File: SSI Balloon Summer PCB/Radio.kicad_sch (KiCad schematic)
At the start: 16 parts, among them J3 LoRa antenna, J4 APRS antenna, U1 RFM95W-915S2, U5 DRA818V

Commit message: Fixed ERC - no ERC errors
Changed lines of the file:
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@@
 	)
 	(junction
+		(at 116.84 111.76)
+		(diameter 0)
+		(color 0 0 0 0)
+	)
+	(junction
 		(at 196.85 80.01)
 		(diameter 0)
@@
 		)
 	)
+	(label "+4V1"
+		(at 250.19 102.87 0)
+		(effects
+			(font
+				(size 1.27 1.27)
+			)
+			(justify left bottom)
+		)
+	)
 	(label "APRS_AUDIO"
 		(at 147.32 80.01 0)
@@
 	)
 	(symbol
-		(lib_id "power:+4V")
-		(at 250.19 102.87 0)
-		(unit 1)
-		(body_style 1)
-		(exclude_from_sim no)
-		(in_bom yes)
-		(on_board yes)
-		(in_pos_files yes)
-		(dnp no)
-		(fields_autoplaced yes)
-		(property "Reference" "#PWR074"
-			(at 250.19 106.68 0)
-			(hide yes)
-			(show_name no)
-			(do_not_autoplace no)
-			(effects
-				(font
-					(size 1.27 1.27)
-				)
-			)
-		)
-		(property "Value" "+4V1"
-			(at 250.19 97.79 0)
-			(show_name no)
-			(do_not_autoplace no)
-			(effects
-				(font
-					(size 1.27 1.27)
-				)
-			)
-		)
-		(property "Footprint" ""
-			(at 250.19 102.87 0)
-			(hide yes)
-			(show_name no)
-			(do_not_autoplace no)
-			(effects
-				(font
-					(size 1.27 1.27)
-				)
-			)
-		)
-		(property "Datasheet" ""
-			(at 250.19 102.87 0)
-			(hide yes)
-			(show_name no)
-			(do_not_autoplace no)
-			(effects
-				(font
-					(size 1.27 1.27)
-				)
-			)
-		)
-		(property "Description" "Power symbol creates a global label with name \"+4V1\""
-			(at 250.19 102.87 0)
-			(hide yes)
-			(show_name no)
-			(do_not_autoplace no)
-			(effects
-				(font
-					(size 1.27 1.27)
-				)
-			)
-		)
-		(pin "1"
-		)
-		(instances
-			(project "SSI Summer Balloons"
-				(path "/3c45a535-6e6b-4825-ad52-82c10cbe7866/2467bfc8-9a58-45c6-9683-5b5ac73ee36d"
-					(reference "#PWR074")
-					(unit 1)
-				)
-			)
-		)
-	)
-	(symbol
 		(lib_id "power:GND")
 		(at 201.93 91.44 0)
@@
 					(unit 1)
 				)
+			)
+		)
+	)
+	(symbol
+		(lib_id "power:PWR_FLAG")
+		(at 116.84 111.76 0)
+		(unit 1)
+		(body_style 1)
+		(exclude_from_sim no)
+		(in_bom yes)
+		(on_board yes)
+		(in_pos_files yes)
+		(dnp no)
+		(fields_autoplaced yes)
+		(property "Reference" "#FLG05"
+			(at 116.84 109.855 0)
+			(hide yes)
+			(show_name no)
+			(do_not_autoplace no)
+			(effects
+				(font
+					(size 1.27 1.27)
+				)
+			)
+		)
+		(property "Value" "PWR_FLAG"
+			(at 116.84 106.68 0)
+			(show_name no)
+			(do_not_autoplace no)
+			(effects
+				(font
+					(size 1.27 1.27)
+				)
+			)
+		)
+		(property "Footprint" ""
+			(at 116.84 111.76 0)
+			(hide yes)
+			(show_name no)
+			(do_not_autoplace no)
+			(effects
+				(font
+					(size 1.27 1.27)
+				)
+			)
+		)
+		(property "Datasheet" ""
+			(at 116.84 111.76 0)
+			(hide yes)
+			(show_name no)
+			(do_not_autoplace no)
+			(effects
+				(font
+					(size 1.27 1.27)
+				)
+			)
+		)
+		(property "Description" "Special symbol for telling ERC where power comes from"
+			(at 116.84 111.76 0)
+			(hide yes)
+			(show_name no)
+			(do_not_autoplace no)
+			(effects
+				(font
+					(size 1.27 1.27)
+				)
+			)
+		)
+		(pin "1"
+		)
+		(instances
+			(project "SSI Summer Balloons"
+				(path "/3c45a535-6e6b-4825-ad52-82c10cbe7866/2467bfc8-9a58-45c6-9683-5b5ac73ee36d"
+					(reference "#FLG05")
+					(unit 1)
+				)

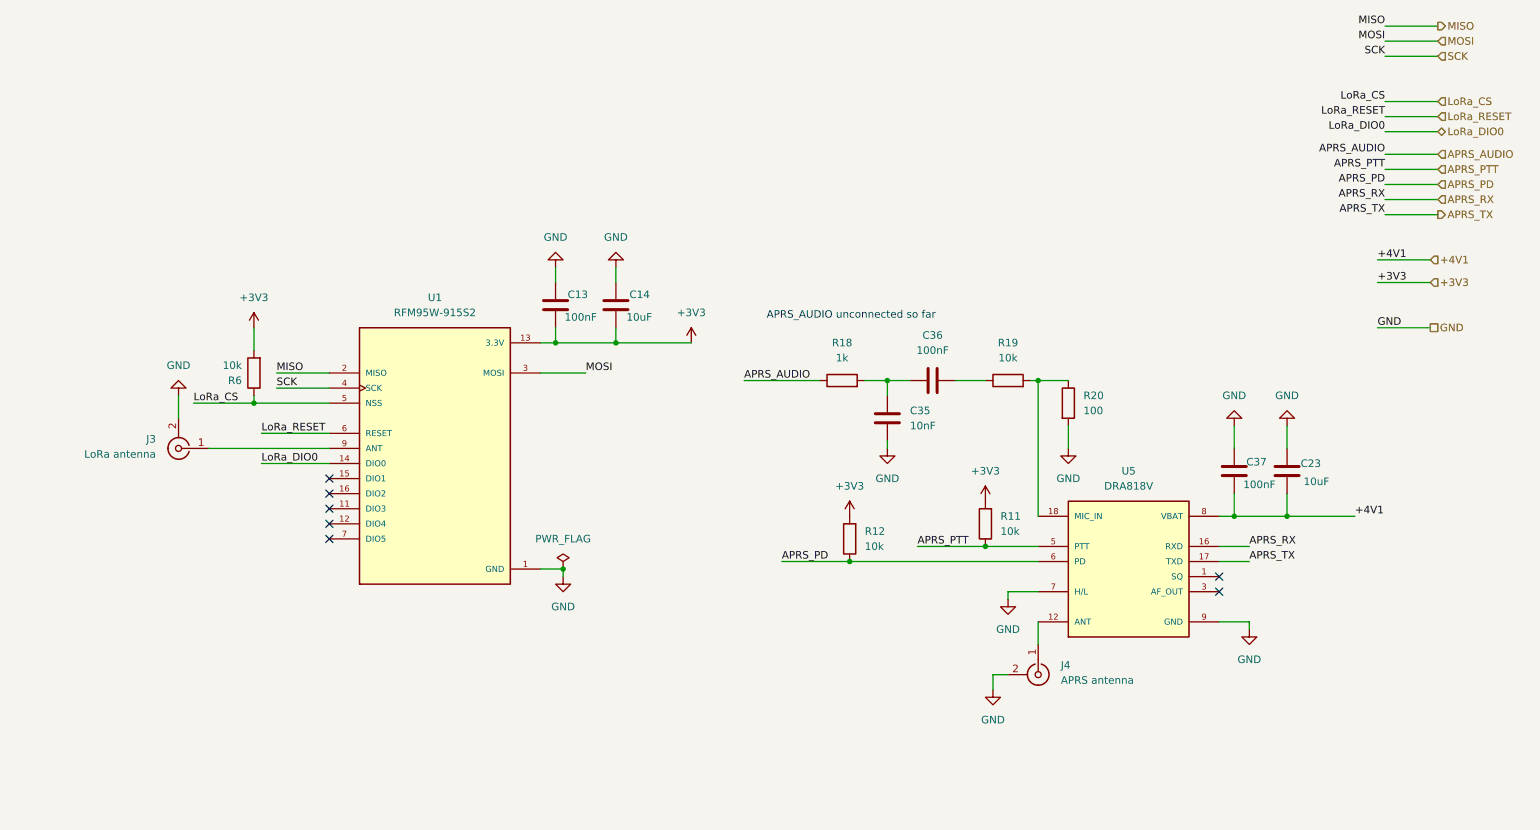
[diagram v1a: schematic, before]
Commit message: Overhauled power symbols for consistency and ERC
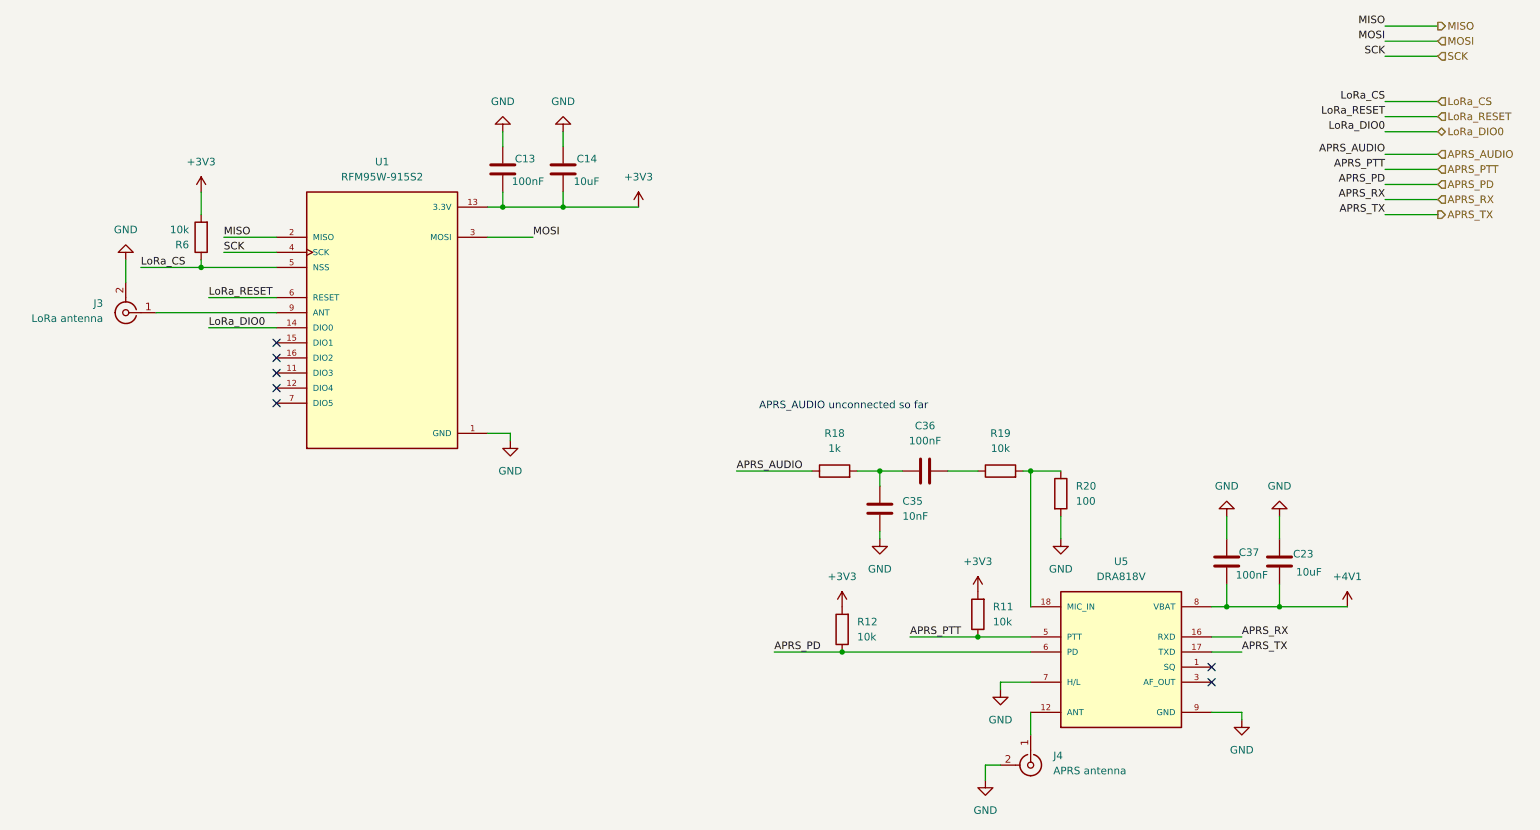
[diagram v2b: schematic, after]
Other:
- moved on the sheet: C13, C14, C23, C35, C36, C37, J3, J4, R11, R12, R18, R19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

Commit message: fixed footprints
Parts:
- C13, C35, C36, C37: footprint (none) -> Capacitor_SMD:C_0603_1608Metric
- C14, C23: footprint (none) -> Capacitor_SMD:C_0805_2012Metric
- J3, J4: footprint (none) -> Connector_Coaxial:U.FL_Hirose_U.FL-R-SMT-1_Vertical
- R11, R12, R18, R19, R20, R6: footprint (none) -> Resistor_SMD:R_0603_1608Metric
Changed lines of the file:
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@@
 			)
 		)
-		(property "Footprint" ""
+		(property "Footprint" "Resistor_SMD:R_0603_1608Metric"
 			(at 198.882 99.06 90)
 			(hide yes)
@@
 			)
 		)
-		(property "Footprint" ""
+		(property "Footprint" "Resistor_SMD:R_0603_1608Metric"
 			(at 188.468 119.38 90)
 			(hide yes)
@@
 			)
 		)
-		(property "Footprint" ""
+		(property "Footprint" "Capacitor_SMD:C_0805_2012Metric"
 			(at 117.8052 48.26 0)
 			(hide yes)
@@
 			)
 		)
-		(property "Footprint" ""
+		(property "Footprint" "Connector_Coaxial:U.FL_Hirose_U.FL-R-SMT-1_Vertical"
 			(at 43.18 68.58 0)
 			(hide yes)
@@
 			)
 		)
-		(property "Footprint" ""
+		(property "Footprint" "Connector_Coaxial:U.FL_Hirose_U.FL-R-SMT-1_Vertical"
 			(at 195.58 144.78 0)
 			(hide yes)
@@
 			)
 		)
-		(property "Footprint" ""
+		(property "Footprint" "Resistor_SMD:R_0603_1608Metric"
 			(at 57.658 55.88 90)
 			(hide yes)
@@
 			)
 		)
-		(property "Footprint" ""
+		(property "Footprint" "Resistor_SMD:R_0603_1608Metric"
 			(at 162.56 97.028 90)
 			(hide yes)
@@
 			)
 		)
-		(property "Footprint" ""
+		(property "Footprint" "Capacitor_SMD:C_0603_1608Metric"
 			(at 171.1452 105.41 0)
 			(hide yes)
@@
 			)
 		)
-		(property "Footprint" ""
+		(property "Footprint" "Resistor_SMD:R_0603_1608Metric"
 			(at 190.5 97.028 90)
 			(hide yes)
@@
 			)
 		)
-		(property "Footprint" ""
+		(property "Footprint" "Capacitor_SMD:C_0603_1608Metric"
 			(at 181.61 94.2848 0)
 			(hide yes)
@@
 			)
 		)
-		(property "Footprint" ""
+		(property "Footprint" "Capacitor_SMD:C_0603_1608Metric"
 			(at 229.5652 114.3 0)
 			(hide yes)
@@
 			)
 		)
-		(property "Footprint" ""
+		(property "Footprint" "Resistor_SMD:R_0603_1608Metric"
 			(at 165.608 121.92 90)
 			(hide yes)
@@
 			)
 		)
-		(property "Footprint" ""
+		(property "Footprint" "Capacitor_SMD:C_0603_1608Metric"
 			(at 107.6452 48.26 0)
 			(hide yes)
@@
 			)
 		)
-		(property "Footprint" ""
+		(property "Footprint" "Capacitor_SMD:C_0805_2012Metric"
 			(at 238.4552 114.3 0)
 			(hide yes)
